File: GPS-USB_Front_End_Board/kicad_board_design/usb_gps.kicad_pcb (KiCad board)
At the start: 4 copper layers, 99.1 x 53.3 mm, 89 parts, among them J1 Micro-USB Connector, J3 SMA, P1 CONN_02X12, P2 CONN_01X03, U1 93LCxxB, U2 FT2232HL-REEL, U3 L4931 LDO, U4 MAX8510, U5 MAX8510, U6 MAX2771, U7 SAWTEK-855969, U8 LT1719S6 -- Not Populated, X1 13.368MHz TCXO, Y1 12MHz Crystal

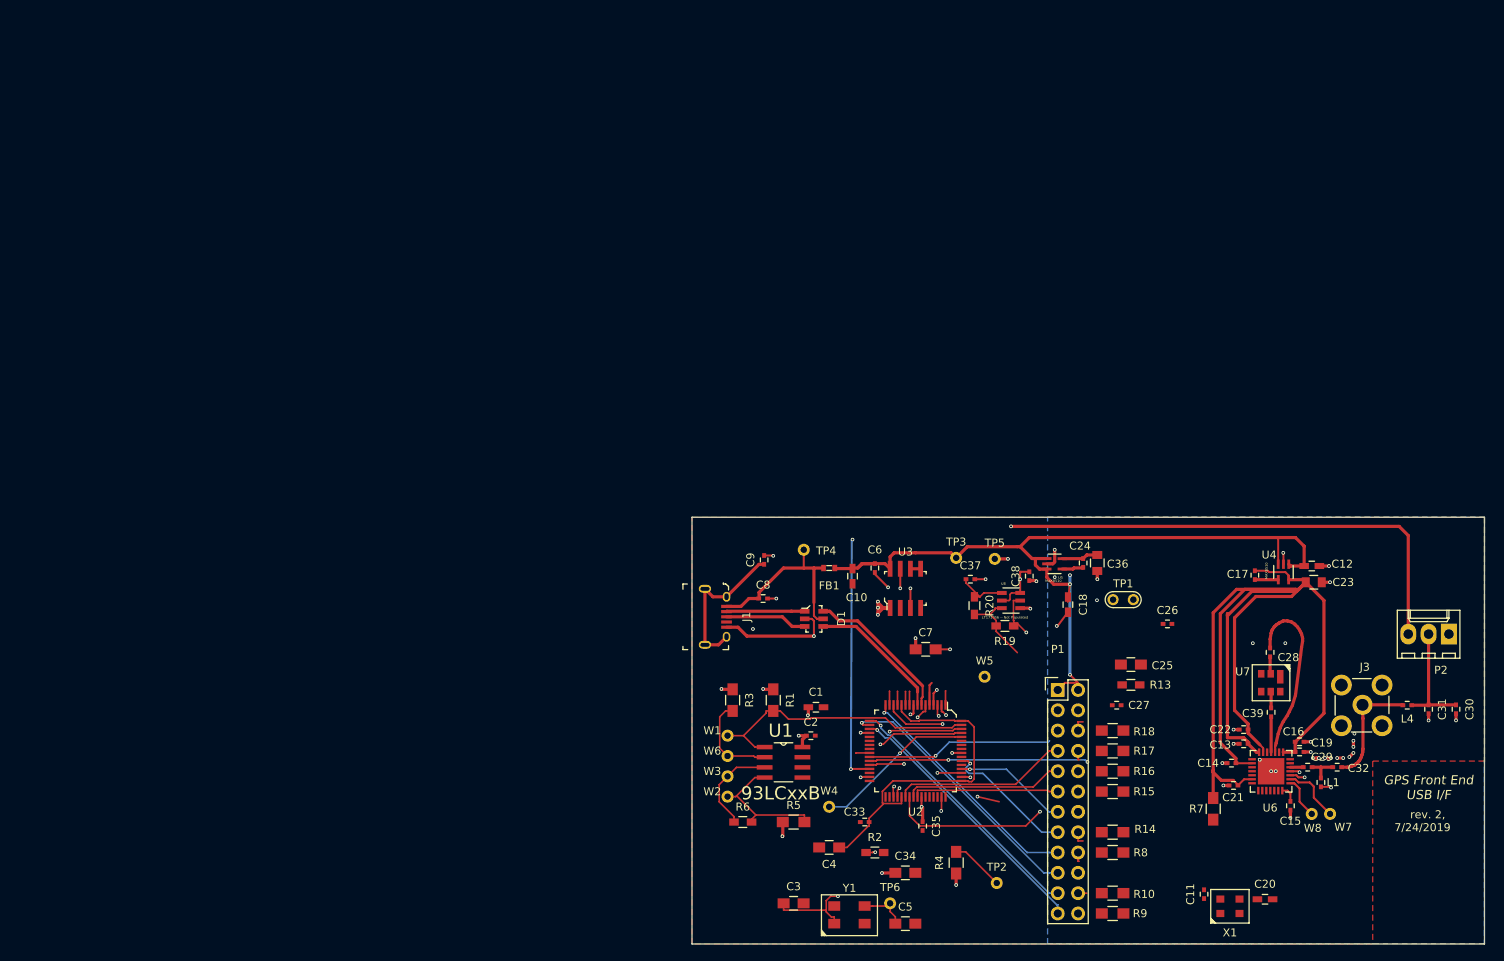
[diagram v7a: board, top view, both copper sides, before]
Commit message: Changed 2.2uF to 10uF. Completed routing. Added via fencing and footprint vias.
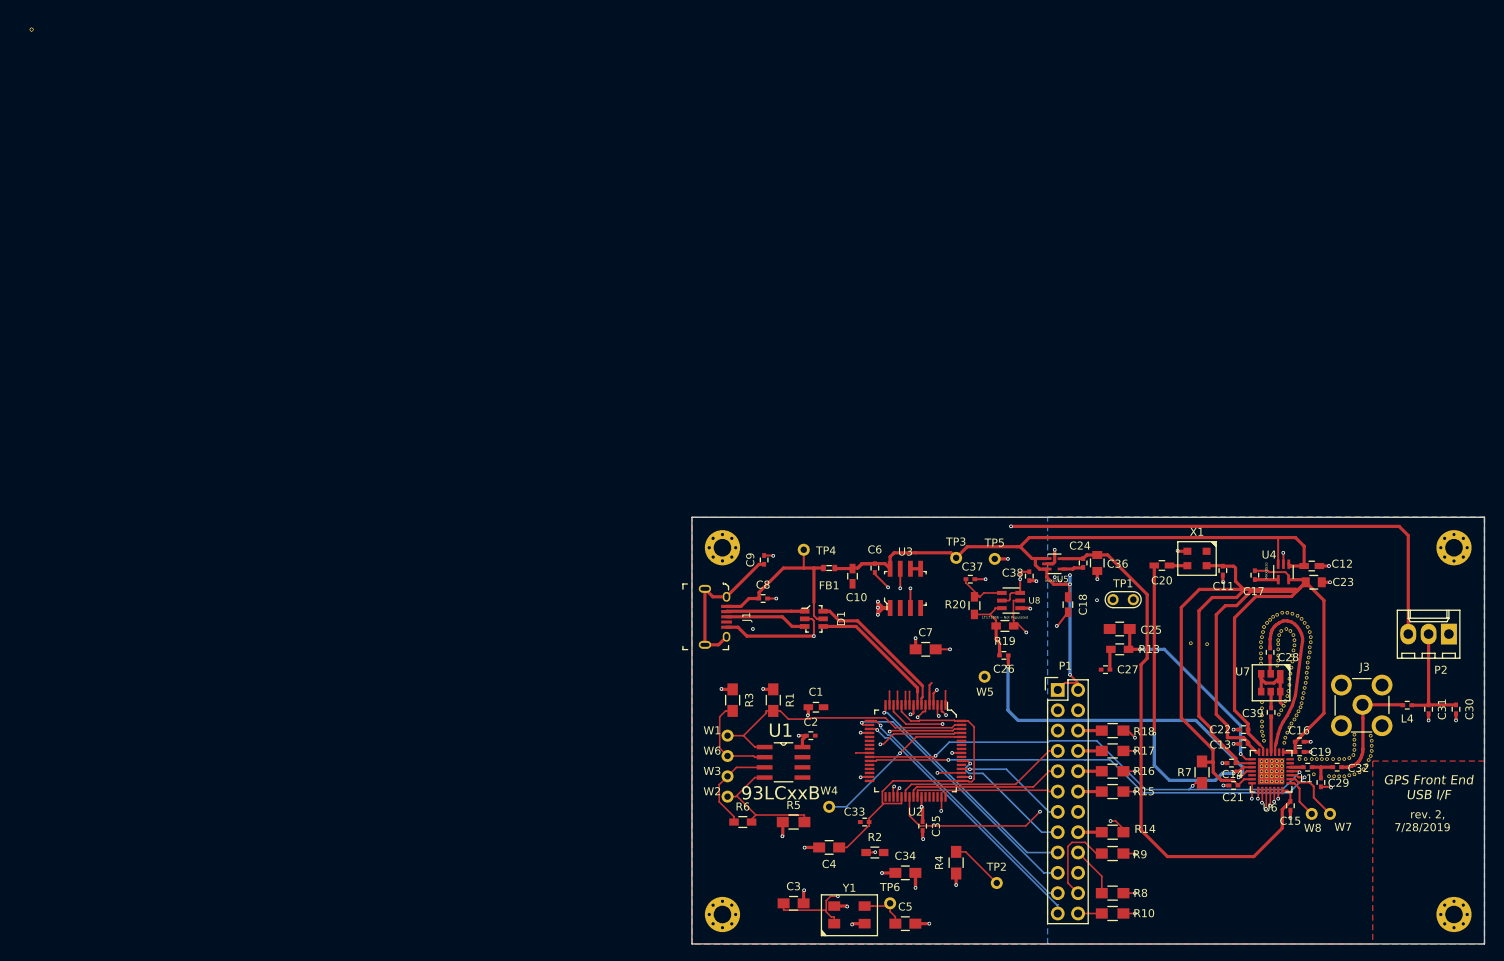
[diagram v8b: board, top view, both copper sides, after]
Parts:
- added REF**: via_10mil, logo:via_10mil, F.Cu at (156.3, 94.0)
- added REF**: via_10mil, logo:via_10mil, F.Cu at (153.7, 93.3)
- added REF**: via_10mil, logo:via_10mil, F.Cu at (159.1, 82.3)
- added REF**: via_10mil, logo:via_10mil, F.Cu at (159.0, 82.9)
- added REF**: via_10mil, logo:via_10mil, F.Cu at (158.9, 83.6)
- added REF**: via_10mil, logo:via_10mil, F.Cu at (158.8, 84.2)
- added REF**: via_10mil, logo:via_10mil, F.Cu at (158.6, 84.7)
- added REF**: via_10mil, logo:via_10mil, F.Cu at (158.4, 85.2)
- added REF**: via_10mil, logo:via_10mil, F.Cu at (158.1, 85.7)
- added REF**: via_10mil, logo:via_10mil, F.Cu at (157.9, 86.2)
- added REF**: via_10mil, logo:via_10mil, F.Cu at (157.5, 86.7)
- added REF**: via_10mil, logo:via_10mil, F.Cu at (157.2, 87.2)
- added REF**: via_10mil, logo:via_10mil, F.Cu at (156.3, 92.7)
- added REF**: via_10mil, logo:via_10mil, F.Cu at (157.0, 87.9)
- added REF**: via_10mil, logo:via_10mil, F.Cu at (156.7, 88.5)
- added REF**: via_10mil, logo:via_10mil, F.Cu at (156.6, 89.2)
- added REF**: via_10mil, logo:via_10mil, F.Cu at (155.7, 79.5)
- added REF**: via_10mil, logo:via_10mil, F.Cu at (155.8, 78.9)
- added REF**: via_10mil, logo:via_10mil, F.Cu at (155.8, 78.2)
- added REF**: via_10mil, logo:via_10mil, F.Cu at (155.8, 77.5)
- added REF**: via_10mil, logo:via_10mil, F.Cu at (155.8, 76.8)
- added REF**: via_10mil, logo:via_10mil, F.Cu at (155.8, 76.3)
- added REF**: via_10mil, logo:via_10mil, F.Cu at (156.0, 75.7)
- added REF**: via_10mil, logo:via_10mil, F.Cu at (155.7, 92.7)
- added REF**: via_10mil, logo:via_10mil, F.Cu at (156.2, 75.2)
- added REF**: via_10mil, logo:via_10mil, F.Cu at (156.8, 74.9)
- added REF**: via_10mil, logo:via_10mil, F.Cu at (157.4, 75.2)
- added REF**: via_10mil, logo:via_10mil, F.Cu at (157.7, 75.7)
- added REF**: via_10mil, logo:via_10mil, F.Cu at (157.9, 76.3)
- added REF**: via_10mil, logo:via_10mil, F.Cu at (157.9, 77.0)
- added REF**: via_10mil, logo:via_10mil, F.Cu at (157.7, 77.6)
- added REF**: via_10mil, logo:via_10mil, F.Cu at (157.6, 78.2)
- added REF**: via_10mil, logo:via_10mil, F.Cu at (157.6, 79.0)
- added REF**: via_10mil, logo:via_10mil, F.Cu at (157.5, 79.8)
- added REF**: via_10mil, logo:via_10mil, F.Cu at (155.0, 92.7)
- added REF**: via_10mil, logo:via_10mil, F.Cu at (157.4, 80.5)
- added REF**: via_10mil, logo:via_10mil, F.Cu at (157.2, 81.2)
- added REF**: via_10mil, logo:via_10mil, F.Cu at (157.2, 81.9)
- added REF**: via_10mil, logo:via_10mil, F.Cu at (157.1, 82.7)
- added REF**: via_10mil, logo:via_10mil, F.Cu at (157.0, 83.3)
- added REF**: via_10mil, logo:via_10mil, F.Cu at (156.7, 83.9)
- added REF**: via_10mil, logo:via_10mil, F.Cu at (156.5, 84.5)
- added REF**: via_10mil, logo:via_10mil, F.Cu at (156.2, 85.1)
- added REF**: via_10mil, logo:via_10mil, F.Cu at (155.9, 85.6)
- added REF** (x2): via_10mil, via_10mil, F.Cu at (0.00, 0.00)
- added REF**: via_10mil, logo:via_10mil, F.Cu at (154.4, 92.7)
- added REF**: MountingHole_2.2mm_M2_Pad_Via, Mounting_Holes:MountingHole_2.2mm_M2_Pad_Via, F.Cu at (86.4, 64.8)
- added REF**: via_10mil, logo:via_10mil, F.Cu at (153.7, 92.7)
- added REF**: via_10mil, logo:via_10mil, F.Cu at (156.3, 92.1)
- added REF**: via_10mil, logo:via_10mil, F.Cu at (155.7, 92.1)
- added REF**: via_10mil, logo:via_10mil, F.Cu at (155.0, 92.1)
- added REF**: via_10mil, logo:via_10mil, F.Cu at (154.4, 92.1)
- added REF**: via_10mil, logo:via_10mil, F.Cu at (155.7, 94.0)
- added REF**: via_10mil, logo:via_10mil, F.Cu at (153.7, 92.1)
- added REF**: via_10mil, logo:via_10mil, F.Cu at (156.3, 91.4)
- added REF**: via_10mil, logo:via_10mil, F.Cu at (155.7, 91.4)
- added REF**: via_10mil, logo:via_10mil, F.Cu at (155.0, 91.4)
- added REF**: via_10mil, logo:via_10mil, F.Cu at (154.4, 91.4)
- added REF**: via_10mil, logo:via_10mil, F.Cu at (153.7, 91.4)
- added REF**: via_10mil, logo:via_10mil, F.Cu at (158.5, 91.2)
- added REF**: via_10mil, logo:via_10mil, F.Cu at (146.9, 76.8)
- added REF**: via_10mil, logo:via_10mil, F.Cu at (144.9, 76.7)
- added REF**: MountingHole_2.2mm_M2_Pad_Via, Mounting_Holes:MountingHole_2.2mm_M2_Pad_Via, F.Cu at (177.8, 64.8)
- added REF**: via_10mil, logo:via_10mil, F.Cu at (155.0, 94.0)
- added REF**: MountingHole_2.2mm_M2_Pad_Via, Mounting_Holes:MountingHole_2.2mm_M2_Pad_Via, F.Cu at (177.8, 110.6)
- added REF**: MountingHole_2.2mm_M2_Pad_Via, Mounting_Holes:MountingHole_2.2mm_M2_Pad_Via, F.Cu at (86.4, 110.6)
- added REF**: via_10mil, logo:via_10mil, F.Cu at (160.3, 93.1)
- added REF**: via_10mil, logo:via_10mil, F.Cu at (162.2, 93.3)
- added REF**: via_10mil, logo:via_10mil, F.Cu at (162.8, 93.3)
- added REF**: via_10mil, logo:via_10mil, F.Cu at (163.4, 93.3)
- added REF**: via_10mil, logo:via_10mil, F.Cu at (164.1, 93.3)
- added REF**: via_10mil, logo:via_10mil, F.Cu at (164.7, 93.2)
- added REF**: via_10mil, logo:via_10mil, F.Cu at (165.4, 93.1)
- added REF**: via_10mil, logo:via_10mil, F.Cu at (166.0, 92.8)
- added REF**: via_10mil, logo:via_10mil, F.Cu at (154.4, 94.0)
- added REF**: via_10mil, logo:via_10mil, F.Cu at (166.5, 92.5)
- added REF**: via_10mil, logo:via_10mil, F.Cu at (166.9, 91.9)
- added REF**: via_10mil, logo:via_10mil, F.Cu at (167.1, 91.3)
- added REF**: via_10mil, logo:via_10mil, F.Cu at (167.4, 90.8)
- added REF**: via_10mil, logo:via_10mil, F.Cu at (167.5, 90.2)
- added REF**: via_10mil, logo:via_10mil, F.Cu at (167.5, 89.5)
- added REF**: via_10mil, logo:via_10mil, F.Cu at (167.5, 88.9)
- added REF**: via_10mil, logo:via_10mil, F.Cu at (167.4, 88.3)
- added REF**: via_10mil, logo:via_10mil, F.Cu at (159.3, 91.2)
- added REF**: via_10mil, logo:via_10mil, F.Cu at (160.0, 91.2)
- added REF**: via_10mil, logo:via_10mil, F.Cu at (153.7, 94.0)
- added REF**: via_10mil, logo:via_10mil, F.Cu at (160.7, 91.2)
- added REF**: via_10mil, logo:via_10mil, F.Cu at (161.3, 91.2)
- added REF**: via_10mil, logo:via_10mil, F.Cu at (161.9, 91.2)
- added REF**: via_10mil, logo:via_10mil, F.Cu at (162.7, 91.2)
- added REF**: via_10mil, logo:via_10mil, F.Cu at (163.4, 91.2)
- added REF**: via_10mil, logo:via_10mil, F.Cu at (164.1, 91.2)
- added REF**: via_10mil, logo:via_10mil, F.Cu at (164.7, 91.1)
- added REF**: via_10mil, logo:via_10mil, F.Cu at (165.2, 90.7)
- added REF**: via_10mil, logo:via_10mil, F.Cu at (165.4, 90.0)
- added REF**: via_10mil, logo:via_10mil, F.Cu at (165.4, 89.4)
- added REF**: via_10mil, logo:via_10mil, F.Cu at (156.3, 93.3)
- added REF**: via_10mil, logo:via_10mil, F.Cu at (165.4, 88.8)
- added REF**: via_10mil, logo:via_10mil, F.Cu at (165.4, 88.1)
- added REF**: via_10mil, logo:via_10mil, F.Cu at (154.1, 88.9)
- added REF**: via_10mil, logo:via_10mil, F.Cu at (153.9, 88.3)
- added REF**: via_10mil, logo:via_10mil, F.Cu at (153.8, 87.8)
- added REF**: via_10mil, logo:via_10mil, F.Cu at (153.8, 87.1)
- added REF**: via_10mil, logo:via_10mil, F.Cu at (153.8, 86.5)
- added REF**: via_10mil, logo:via_10mil, F.Cu at (153.8, 85.7)
- added REF**: via_10mil, logo:via_10mil, F.Cu at (153.8, 84.8)
- added REF**: via_10mil, logo:via_10mil, F.Cu at (153.8, 84.1)
- added REF**: via_10mil, logo:via_10mil, F.Cu at (155.7, 93.3)
- added REF**: via_10mil, logo:via_10mil, F.Cu at (153.7, 79.2)
- added REF**: via_10mil, logo:via_10mil, F.Cu at (153.7, 78.6)
- added REF**: via_10mil, logo:via_10mil, F.Cu at (153.7, 78.0)
- added REF**: via_10mil, logo:via_10mil, F.Cu at (153.7, 77.2)
- added REF**: via_10mil, logo:via_10mil, F.Cu at (153.7, 76.6)
- added REF**: via_10mil, logo:via_10mil, F.Cu at (153.8, 75.9)
- added REF**: via_10mil, logo:via_10mil, F.Cu at (153.9, 75.3)
- added REF**: via_10mil, logo:via_10mil, F.Cu at (154.1, 74.7)
- added REF**: via_10mil, logo:via_10mil, F.Cu at (154.4, 74.2)
- added REF**: via_10mil, logo:via_10mil, F.Cu at (154.8, 73.8)
- added REF**: via_10mil, logo:via_10mil, F.Cu at (155.0, 93.3)
- added REF**: via_10mil, logo:via_10mil, F.Cu at (155.2, 73.4)
- added REF**: via_10mil, logo:via_10mil, F.Cu at (155.7, 73.2)
- added REF**: via_10mil, logo:via_10mil, F.Cu at (156.3, 72.9)
- added REF**: via_10mil, logo:via_10mil, F.Cu at (157.0, 72.9)
- added REF**: via_10mil, logo:via_10mil, F.Cu at (157.6, 73.0)
- added REF**: via_10mil, logo:via_10mil, F.Cu at (158.2, 73.3)
- added REF**: via_10mil, logo:via_10mil, F.Cu at (158.8, 73.7)
- added REF**: via_10mil, logo:via_10mil, F.Cu at (159.1, 74.2)
- added REF**: via_10mil, logo:via_10mil, F.Cu at (159.5, 74.7)
- added REF**: via_10mil, logo:via_10mil, F.Cu at (159.8, 75.3)
- added REF**: via_10mil, logo:via_10mil, F.Cu at (154.4, 93.3)
- added REF**: via_10mil, logo:via_10mil, F.Cu at (159.9, 75.9)
- added REF**: via_10mil, logo:via_10mil, F.Cu at (159.9, 76.6)
- added REF**: via_10mil, logo:via_10mil, F.Cu at (159.8, 77.2)
- added REF**: via_10mil, logo:via_10mil, F.Cu at (159.8, 77.9)
- added REF**: via_10mil, logo:via_10mil, F.Cu at (159.6, 78.5)
- added REF**: via_10mil, logo:via_10mil, F.Cu at (159.5, 79.1)
- added REF**: via_10mil, logo:via_10mil, F.Cu at (159.5, 79.8)
- added REF**: via_10mil, logo:via_10mil, F.Cu at (159.4, 80.4)
- added REF**: via_10mil, logo:via_10mil, F.Cu at (159.4, 81.0)
- added REF**: via_10mil, logo:via_10mil, F.Cu at (159.3, 81.7)
- moved X1 45.3 mm to (146.9, 65.2), turned to 180 degrees
- moved C20 43.7 mm to (141.3, 67.0), turned to 180 degrees
- moved C11 40.5 mm to (148.9, 67.6), turned to 270 degrees
- moved C26 20.8 mm to (121.5, 78.2), turned to 180 degrees
- moved R8 5.08 mm to (135.1, 108.0)
- moved R9 4.95 mm to (135.1, 103.0)
- moved R7 4.78 mm to (146.3, 92.8)
- moved R13 4.66 mm to (136.0, 77.5)
- moved C25 4.66 mm to (136.0, 74.9)
- moved C27 4.66 mm to (134.2, 80.0)
- turned R16 to 180 degrees
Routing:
- net /MAX_2769/VCCD: track 6.86 -> 69.2 mm
- net Net-(C26-Pad1): track 0.00 -> 42.6 mm, vias 0 -> 2
- net Net-(C20-Pad2): track 0.00 -> 38.7 mm, vias 0 -> 2
- net /USB_FT2232/GPIO0: track 24.6 -> 61.2 mm, vias 2 -> 3
- net Net-(U2-Pad29): track 31.1 -> 0.00 mm, vias 2 -> 0
- net /MAX_2769/CS#: track 0.00 -> 30.1 mm, vias 0 -> 2
- net /USB_FT2232/GPIO1: track 29.3 -> 58.9 mm, vias 3 -> 2
- net /MAX_2769/I1: track 0.00 -> 28.7 mm, vias 0 -> 2
- net /MAX_2769/SCLKL: track 0.00 -> 27.6 mm, vias 0 -> 2
- net GND: track 88.9 -> 116.0 mm, vias 31 -> 37
- net Net-(C25-Pad1): track 0.00 -> 25.8 mm, vias 0 -> 2
- net /MAX_2769/SDATA: track 0.00 -> 23.8 mm, vias 0 -> 2
- net /MAX_2769/I0: track 0.00 -> 23.7 mm, vias 0 -> 2
- net /MAX_2769/Q0: track 0.00 -> 22.9 mm, vias 0 -> 2
- net /MAX_2769/Q1: track 0.00 -> 21.9 mm, vias 0 -> 2
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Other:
- board text added: "rev. 2, 7/28/2019"
- board text removed: "rev. 2, 7/24/2019"
